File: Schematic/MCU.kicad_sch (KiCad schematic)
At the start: 21 parts, among them IC3 STM32H743VIT6, J1 USB_C_Receptacle_USB2.0_16P, SW1 TS24CA, Y1 8MHz

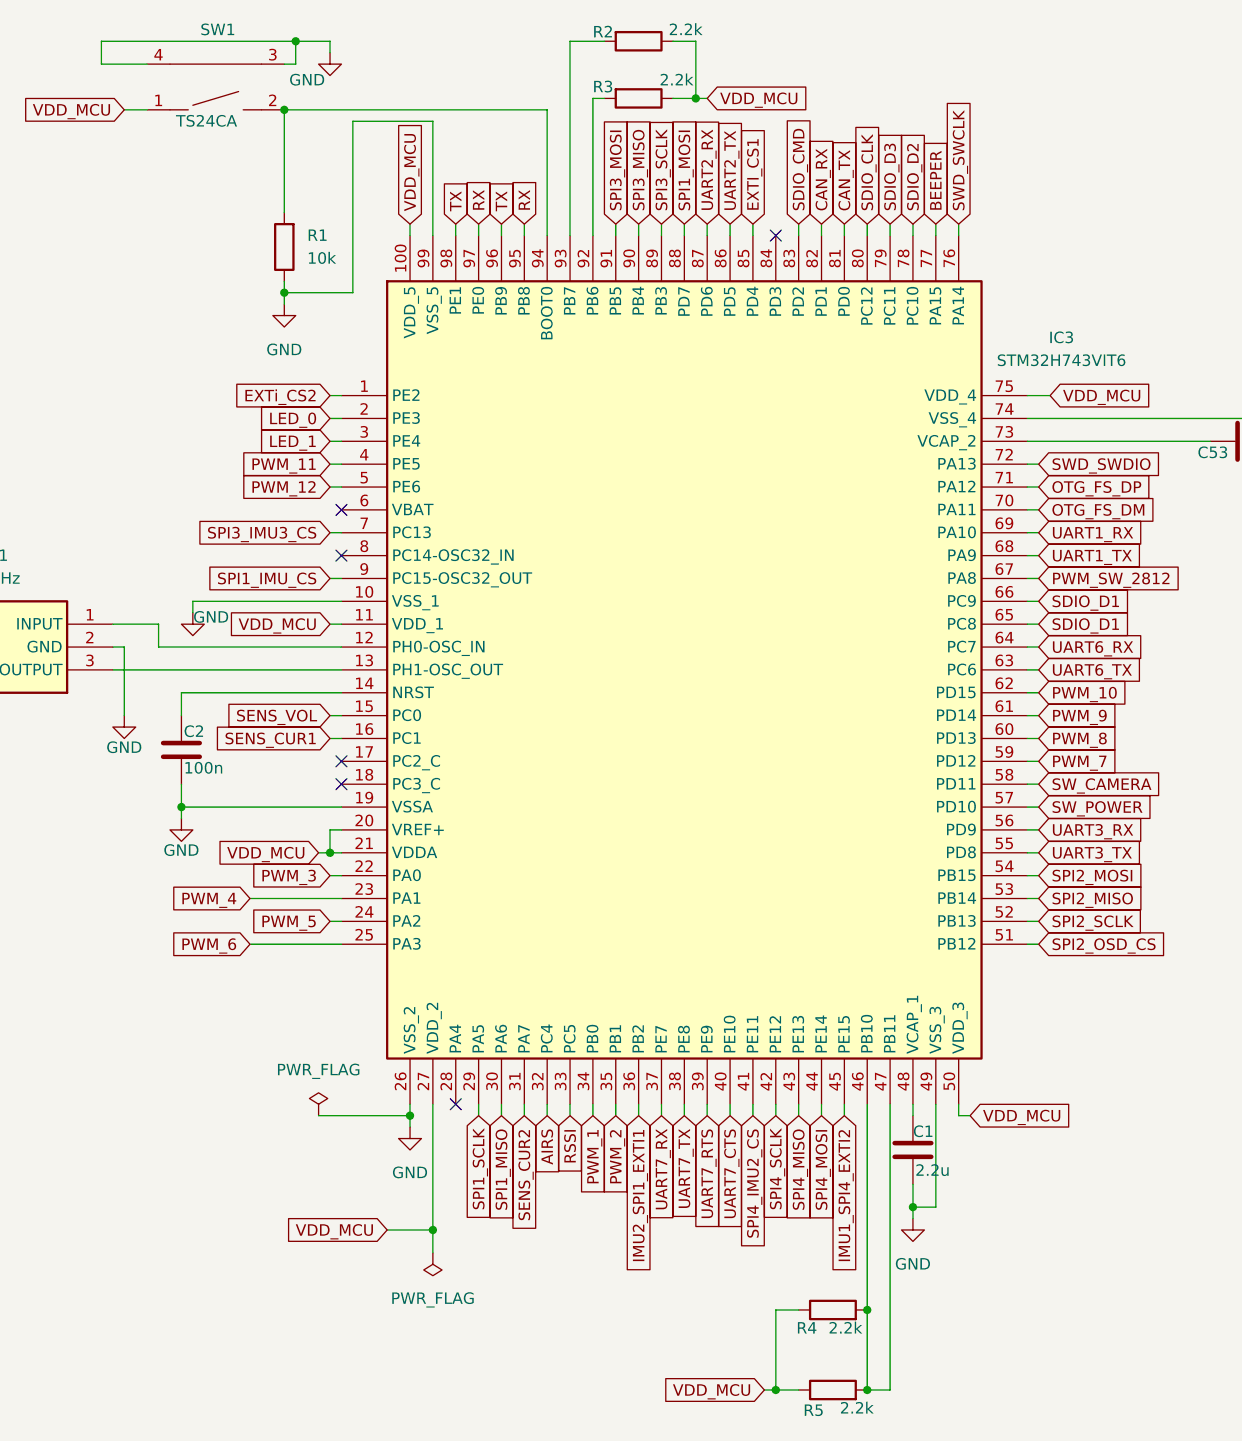
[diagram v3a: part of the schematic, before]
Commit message: Refactor fp-lib-table: Remove unused libraries and update description for fch7_fp
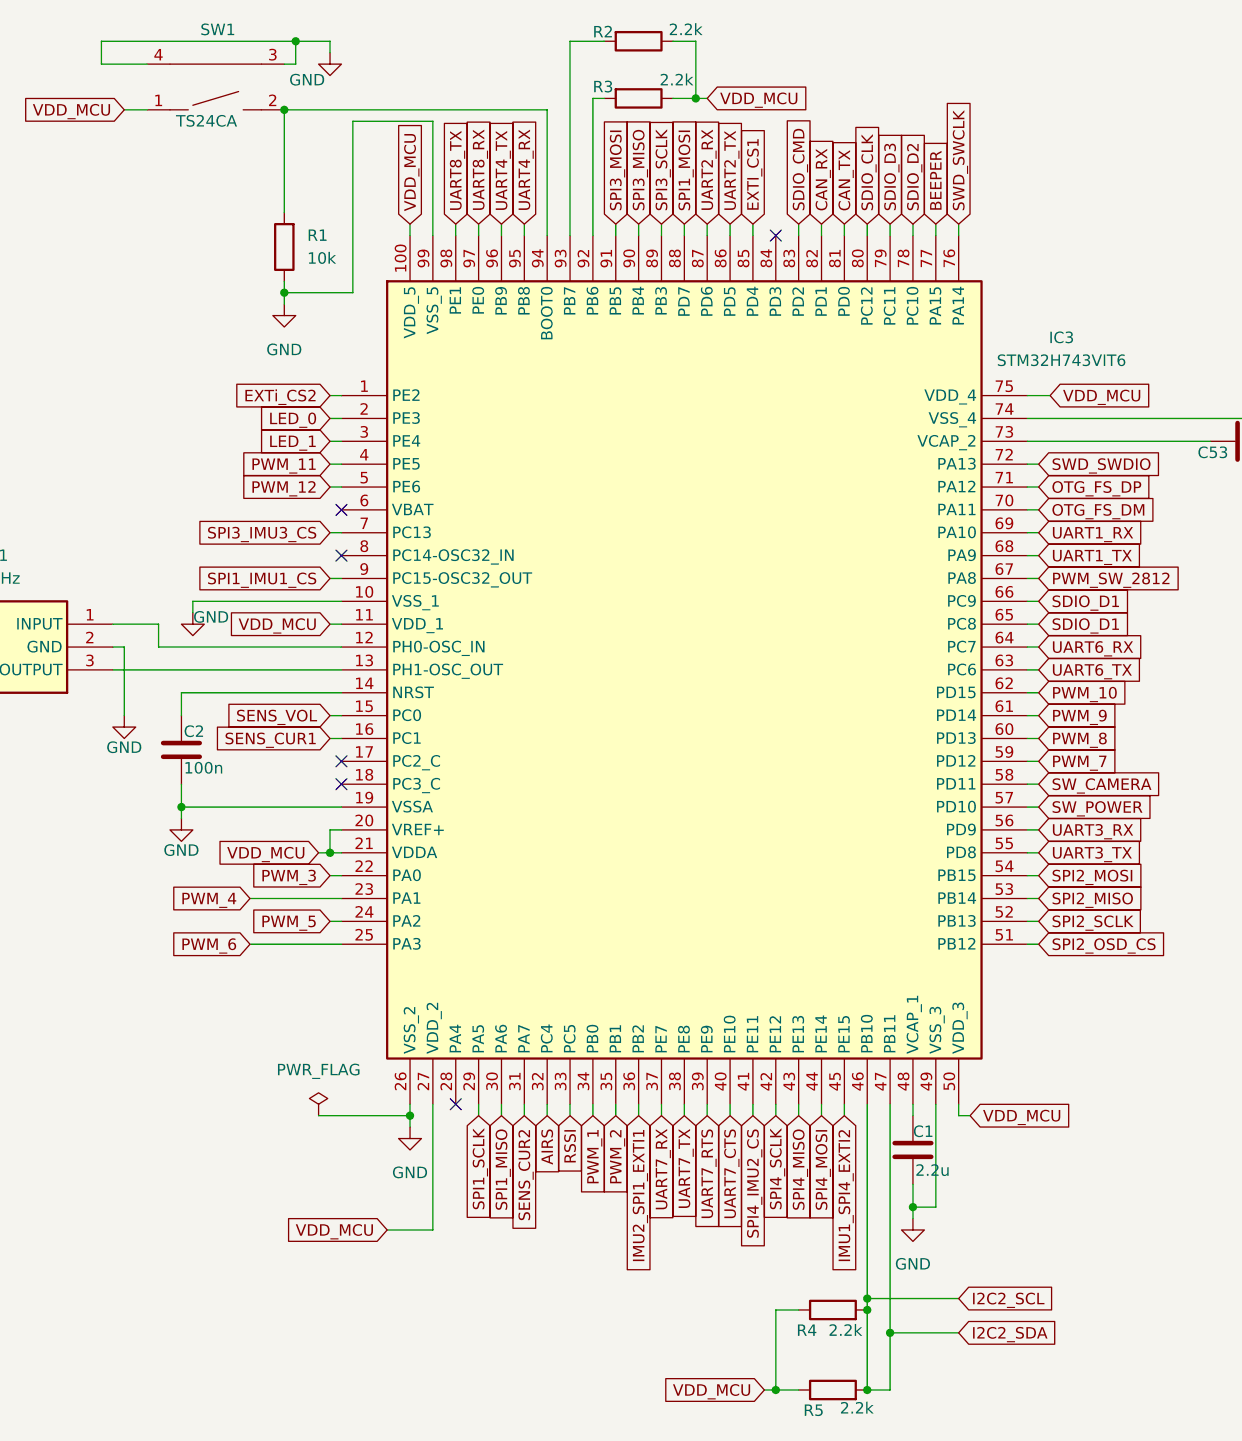
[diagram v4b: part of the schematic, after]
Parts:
- SW1: footprint ProLib_pcs_2025-11-24:SW-SMD_2P-TS24CA -> fch7_fp:SW-SMD_2P-TS24CA
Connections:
- net I2C2_SCL: now reaches IC3.46 (PB10), IC3.47 (PB11), R4.2, R5.2
- net RX renamed UART4_RX
- net UART4_RX: no longer IC3.97 (PE0)
- net SPI1_IMU_CS renamed SPI1_IMU1_CS
- net TX renamed UART4_TX
- net UART4_TX: no longer IC3.98 (PE1)
- new net UART8_RX: IC3.97 (PE0)
- new net UART8_TX: IC3.98 (PE1)
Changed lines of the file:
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@@
 	)
 	(junction
-		(at 228.6 85.09)
+		(at 124.46 172.72)
 		(diameter 0)
 		(color 0 0 0 0)
 	)
 	(junction
-		(at 73.66 161.29)
+		(at 228.6 85.09)
 		(diameter 0)
 		(color 0 0 0 0)
@@
 	)
 	(junction
+		(at 121.92 168.91)
+		(diameter 0)
+		(color 0 0 0 0)
+	)
+	(junction
 		(at 62.23 119.38)
 		(diameter 0)
@@
 	(wire
 		(pts
+			(xy 121.92 168.91) (xy 121.92 170.18)
+		)
+		(stroke
+			(width 0)
+			(type default)
+		)
+	)
+	(wire
+		(pts
 			(xy 46.99 91.44) (xy 63.5 91.44)
 		)
@@
 	(wire
 		(pts
-			(xy 73.66 161.29) (xy 73.66 163.83)
-		)
-		(stroke
-			(width 0)
-			(type default)
-		)
-	)
-	(wire
-		(pts
 			(xy 64.77 57.15) (xy 57.15 57.15)
 		)
@@
 	(wire
 		(pts
+			(xy 121.92 168.91) (xy 132.08 168.91)
+		)
+		(stroke
+			(width 0)
+			(type default)
+		)
+	)
+	(wire
+		(pts
 			(xy 100.33 35.56) (xy 102.87 35.56)
 		)
@@
 	(wire
 		(pts
-			(xy 121.92 147.32) (xy 121.92 170.18)
+			(xy 121.92 147.32) (xy 121.92 168.91)
 		)
 		(stroke
@@
 	(wire
 		(pts
-			(xy 124.46 147.32) (xy 124.46 179.07)
+			(xy 127 158.75) (xy 129.54 158.75)
 		)
 		(stroke
@@
 	(wire
 		(pts
-			(xy 127 158.75) (xy 129.54 158.75)
+			(xy 124.46 172.72) (xy 132.08 172.72)
 		)
 		(stroke
@@
 	(wire
 		(pts
+			(xy 124.46 172.72) (xy 124.46 179.07)
+		)
+		(stroke
+			(width 0)
+			(type default)
+		)
+	)
+	(wire
+		(pts
 			(xy 262.89 85.09) (xy 264.16 85.09)
 		)
@@
 	(wire
 		(pts
+			(xy 124.46 147.32) (xy 124.46 172.72)
+		)
+		(stroke
+			(width 0)
+			(type default)
+		)
+	)
+	(wire
+		(pts
 			(xy 104.14 49.53) (xy 104.14 50.8)
 		)
@@
 		)
 	)
-	(global_label "RX"
+	(global_label "UART8_RX"
 		(shape input)
 		(at 78.74 49.53 90)
@@
 		)
 		(property "Intersheetrefs" "${INTERSHEET_REFS}"
-			(at 78.74 44.0653 90)
+			(at 78.74 37.2315 90)
 			(effects
 				(font
@@
 		)
 	)
+	(global_label "I2C2_SDA"
+		(shape input)
+		(at 132.08 172.72 0)
+		(fields_autoplaced yes)
+		(effects
+			(font
+				(size 1.27 1.27)
+			)
+			(justify left)
+		)
+		(property "Intersheetrefs" "${INTERSHEET_REFS}"
+			(at 143.8947 172.72 0)
+			(effects
+				(font
+					(size 1.27 1.27)
+				)
+				(justify left)
+				(hide yes)
+			)
+		)
+	)
 	(global_label "PWM_7"
 		(shape input)
@@
 		)
 	)
-	(global_label "TX"
+	(global_label "UART8_TX"
 		(shape input)
 		(at 76.2 49.53 90)
@@
 		)
 		(property "Intersheetrefs" "${INTERSHEET_REFS}"
-			(at 76.2 44.3677 90)
+			(at 76.2 37.5339 90)
 			(effects
 				(font
@@
 		)
 	)
-	(global_label "RX"
+	(global_label "UART4_RX"
 		(shape input)
 		(at 83.82 49.53 90)
@@
 		)
 		(property "Intersheetrefs" "${INTERSHEET_REFS}"
-			(at 83.82 44.0653 90)
+			(at 83.82 37.2315 90)
 			(effects
 				(font
@@
 		)
 	)
-	(global_label "TX"
+	(global_label "UART4_TX"
 		(shape input)
 		(at 81.28 49.53 90)
@@
 		)
 		(property "Intersheetrefs" "${INTERSHEET_REFS}"
-			(at 81.28 44.3677 90)
+			(at 81.28 37.5339 90)
 			(effects
 				(font
@@
 		)
 	)
-	(global_label "SPI1_IMU_CS"
+	(global_label "SPI1_IMU1_CS"
 		(shape input)
 		(at 62.23 88.9 180)
@@
 		)
 		(property "Intersheetrefs" "${INTERSHEET_REFS}"
-			(at 47.1496 88.9 0)
+			(at 45.9401 88.9 0)
 			(effects
 				(font
@@
 		)
 	)
+	(global_label "I2C2_SCL"
+		(shape input)
+		(at 132.08 168.91 0)
+		(fields_autoplaced yes)
+		(effects
+			(font
+				(size 1.27 1.27)
+			)
+			(justify left)
+		)
+		(property "Intersheetrefs" "${INTERSHEET_REFS}"
+			(at 143.8342 168.91 0)
+			(effects
+				(font
+					(size 1.27 1.27)
+				)
+				(justify left)
+				(hide yes)
+			)
+		)
+	)
 	(global_label "OTG_FS_DP"
 		(shape input)
@@
 			)
 		)
-		(property "Footprint" "ProLib_pcs_2025-11-24:SW-SMD_2P-TS24CA"
+		(property "Footprint" "fch7_fp:SW-SMD_2P-TS24CA"
 			(at 48.768 27.686 0)
 			(effects
@@
 		(dnp no)
 		(property "Reference" "R4"
-			(at 114.046 172.212 90)
+			(at 114.046 172.466 90)
 			(effects
 				(font
@@
 		)
 		(property "Value" "2.2k"
-			(at 117.602 172.212 90)
+			(at 117.602 172.466 90)
 			(effects
 				(font
@@
 					(unit 1)
 				)
-			)
-		)
-	)
-	(symbol
-		(lib_id "power:PWR_FLAG")
-		(at 73.66 163.83 180)
-		(unit 1)
-		(exclude_from_sim no)
-		(in_bom yes)
-		(on_board yes)
-		(dnp no)
-		(fields_autoplaced yes)
-		(property "Reference" "#FLG02"
-			(at 73.66 165.735 0)
-			(effects
-				(font
-					(size 1.27 1.27)
-				)
-				(hide yes)
-			)
-		)
-		(property "Value" "PWR_FLAG"
-			(at 73.66 168.91 0)
-			(effects
-				(font
-					(size 1.27 1.27)
-				)
-			)
-		)
-		(property "Footprint" ""
-			(at 73.66 163.83 0)
-			(effects
-				(font
-					(size 1.27 1.27)
-				)
-				(hide yes)
-			)
-		)
-		(property "Datasheet" "~"
-			(at 73.66 163.83 0)
-			(effects
-				(font
-					(size 1.27 1.27)
-				)
-				(hide yes)
-			)
-		)
-		(property "Description" "Special symbol for telling ERC where power comes from"
-			(at 73.66 163.83 0)
-			(effects
-				(font
-					(size 1.27 1.27)
-				)
-				(hide yes)
-			)
-		)
-		(pin "1"
-		)
-		(instances
-			(project "fch7"
-				(path "/11716af6-0e6e-444b-b738-3f12da23c1a2/0293db95-115d-42d2-990d-f9f4568d02e9"
-					(reference "#FLG02")
-					(unit 1)
-				)
